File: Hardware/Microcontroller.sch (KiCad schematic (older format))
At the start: 30 parts, among them J1 Micro_SD_Card_Det, J2 SWD, J3 Serial, SW1 BOOT, SW2 RST, U1 STM32F103C8Tx, Y1 8M, Y2 32.768k

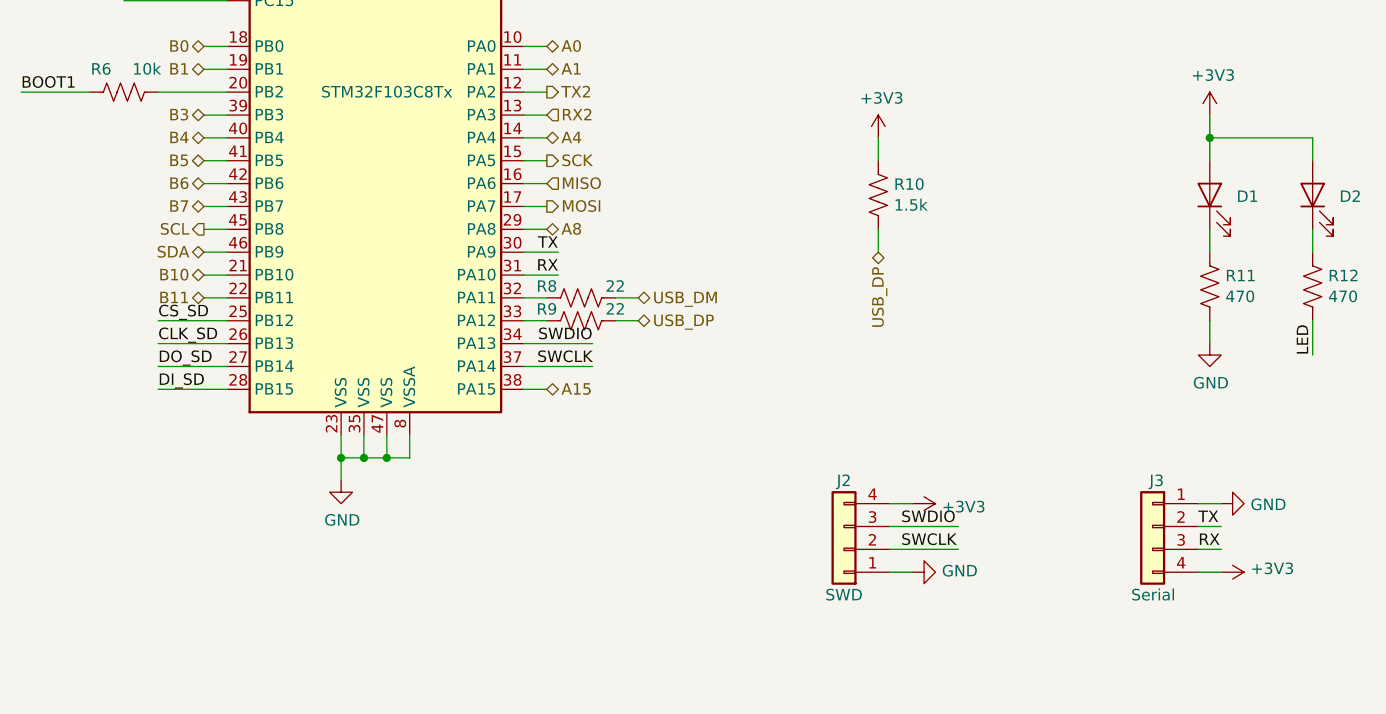
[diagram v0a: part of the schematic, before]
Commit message: Rearranged pins so Serial and I2C are available for external use.
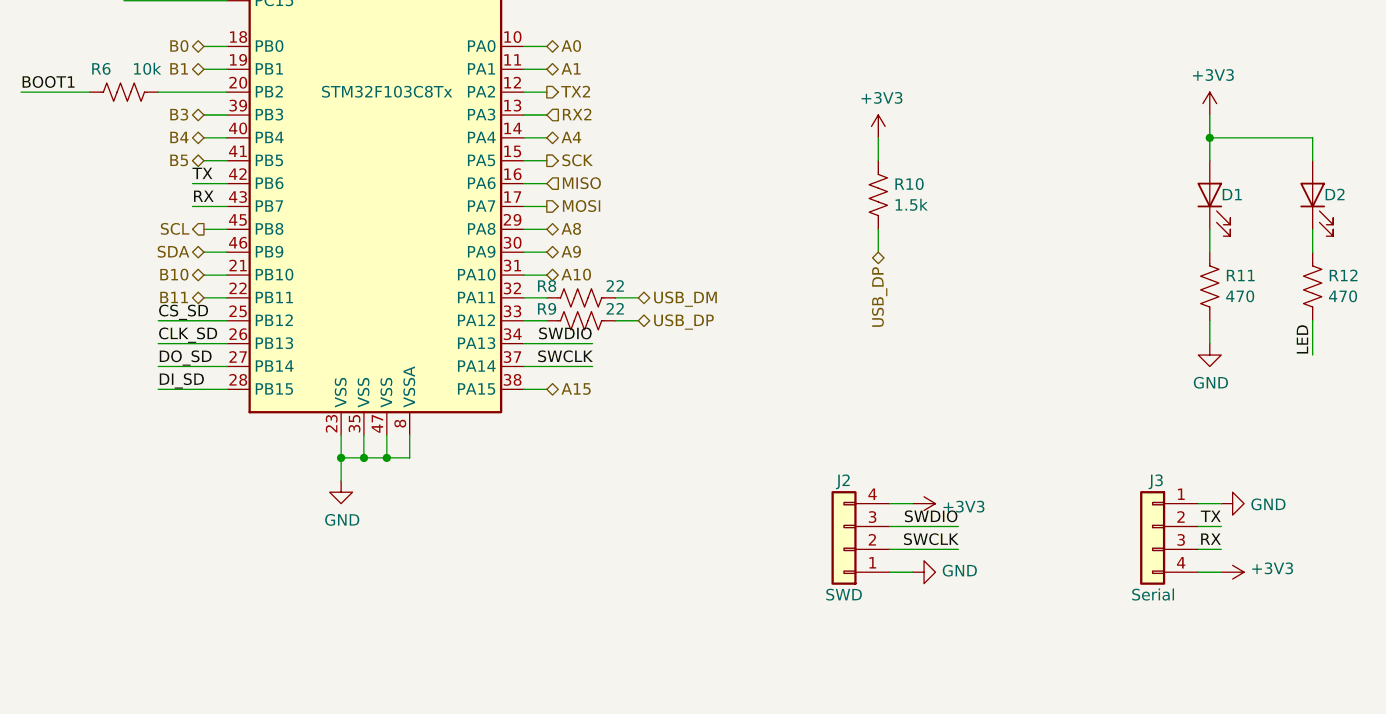
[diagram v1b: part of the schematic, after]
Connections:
- net labels added: A10, A9
- net labels removed: B6, B7
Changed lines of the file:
@@
 	0    1    1    0
 $EndComp
-Text Label 8200 5800 0    50   ~ 0
+Text Label 8450 5800 2    50   ~ 0
 SWCLK
-Text Label 8200 5700 0    50   ~ 0
+Text Label 8450 5700 2    50   ~ 0
 SWDIO
 $Comp
@@
 U 1 1 5EBC4511
 P 9550 4250
-F 0 "D1" V 9543 4133 50  0000 R CNN
+F 0 "D1" V 9550 4200 50  0000 R CNN
 F 1 "LED" V 9498 4133 50  0001 R CNN
 F 2 "LED_SMD:LED_0603_1608Metric" H 9550 4250 50  0001 C CNN
@@
 U 1 1 5EBC49F9
 P 10000 4250
-F 0 "D2" V 9993 4133 50  0000 R CNN
+F 0 "D2" V 10000 4200 50  0000 R CNN
 F 1 "LED" V 9948 4133 50  0001 R CNN
 F 2 "LED_SMD:LED_0603_1608Metric" H 10000 4250 50  0001 C CNN
@@
 	5150 4100 5250 4100
 Wire Wire Line
-	5150 4200 5250 4200
-Wire Wire Line
-	5150 4300 5250 4300
+	5100 4200 5250 4200
+Wire Wire Line
+	5100 4300 5250 4300
 Wire Wire Line
 	1650 4650 1550 4650
@@
 	9600 5900 9500 5900
 Wire Wire Line
-	9600 5700 9500 5700
-Wire Wire Line
 	9600 5800 9500 5800
 $Comp
@@
 	0    1    -1   0
 $EndComp
-Text Label 9500 5700 0    50   ~ 0
+Text Label 9600 5700 2    50   ~ 0
 TX
-Text Label 9500 5800 0    50   ~ 0
+Text Label 9600 5800 2    50   ~ 0
 RX
 Wire Wire Line
-	6550 4500 6700 4500
-Wire Wire Line
-	6550 4600 6700 4600
-Text Label 6700 4600 2    50   ~ 0
+	6550 4500 6650 4500
+Wire Wire Line
+	6550 4600 6650 4600
+Text Label 5100 4300 0    50   ~ 0
 RX
-Text Label 6700 4500 2    50   ~ 0
+Text Label 5100 4200 0    50   ~ 0
 TX
 $Comp
@@
 Text HLabel 5150 4100 0    50   BiDi ~ 0
 B5
-Text HLabel 5150 4200 0    50   BiDi ~ 0
-B6
-Text HLabel 5150 4300 0    50   BiDi ~ 0
-B7
+Text HLabel 6650 4500 2    50   BiDi ~ 0
+A9
+Text HLabel 6650 4600 2    50   BiDi ~ 0
+A10
 Text HLabel 5150 4600 0    50   BiDi ~ 0
 B10
@@
 	-1   0    0    -1
 $EndComp
+Wire Wire Line
+	9600 5700 9500 5700
 $EndSCHEMATC

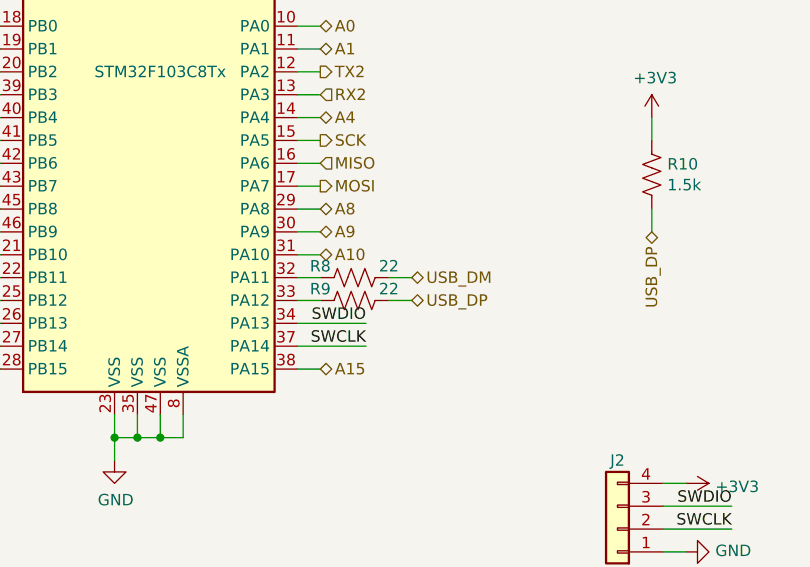
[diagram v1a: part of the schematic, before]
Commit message: Had too many resistors on USB data lines
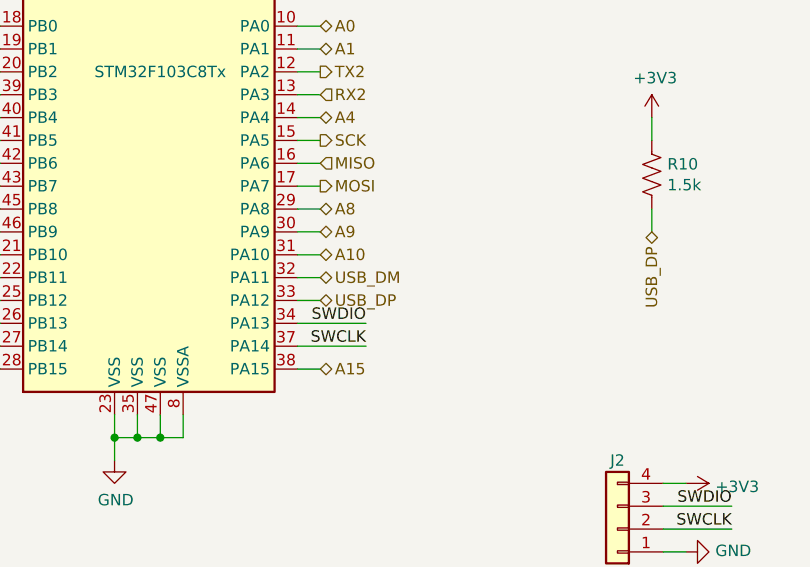
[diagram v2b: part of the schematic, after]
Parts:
- removed R8, R9: 22, Resistor_SMD:R_0603_1608Metric, symbol Device:R_US
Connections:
- net USB_DM: now also U1.32 (PA11)
- net USB_DP: now also U1.33 (PA12)
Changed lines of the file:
@@
 Wire Wire Line
 	6650 4800 6550 4800
-Text HLabel 7050 4700 2    50   BiDi ~ 0
+Text HLabel 6650 4700 2    50   BiDi ~ 0
 USB_DM
-Text HLabel 7050 4800 2    50   BiDi ~ 0
+Text HLabel 6650 4800 2    50   BiDi ~ 0
 USB_DP
 $Comp
@@
 	1    0    0    -1
 $EndComp
-$Comp
-L Device:R_US R8
-U 1 1 5EAD4044
-P 6800 4700
-F 0 "R8" V 6750 4550 50  0000 C CNN
-F 1 "22" V 6750 4850 50  0000 C CNN
-F 2 "Resistor_SMD:R_0603_1608Metric" V 6840 4690 50  0001 C CNN
-F 3 "~" H 6800 4700 50  0001 C CNN
-	1    6800 4700
-	0    1    1    0
-$EndComp
 Wire Wire Line
 	8100 4500 8100 4400
@@
 	8100 4000 8100 4100
 $Comp
-L Device:R_US R9
-U 1 1 5EAD8592
-P 6800 4800
-F 0 "R9" V 6750 4650 50  0000 C CNN
-F 1 "22" V 6750 4950 50  0000 C CNN
-F 2 "Resistor_SMD:R_0603_1608Metric" V 6840 4790 50  0001 C CNN
-F 3 "~" H 6800 4800 50  0001 C CNN
-	1    6800 4800
-	0    1    1    0
-$EndComp
-Wire Wire Line
-	7050 4700 6950 4700
-Wire Wire Line
-	7050 4800 6950 4800
-$Comp
 L Device:C C5
